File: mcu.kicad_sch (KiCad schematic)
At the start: 23 parts, among them J1 USB4105-GF-A-120, U1 STM32G473CEUx, Y1 ECS-240-6-37B-7KM-TR

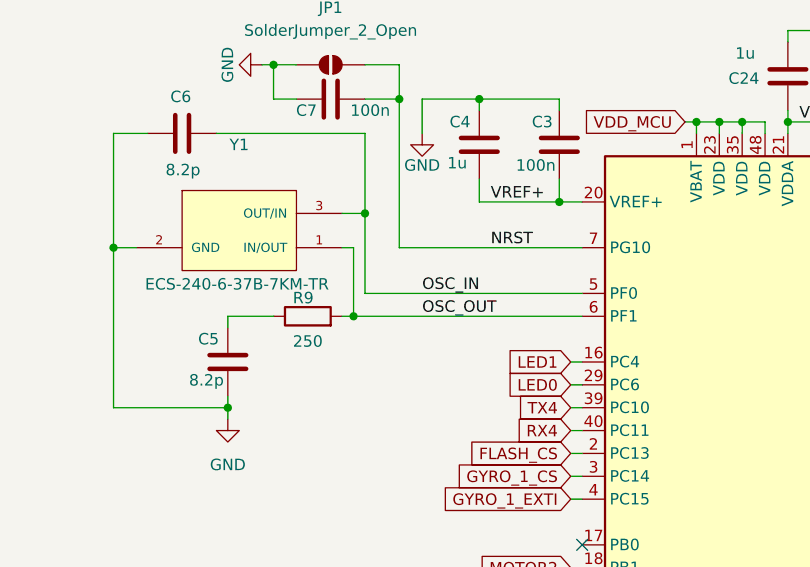
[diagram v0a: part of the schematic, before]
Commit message: Placed every components on one face only
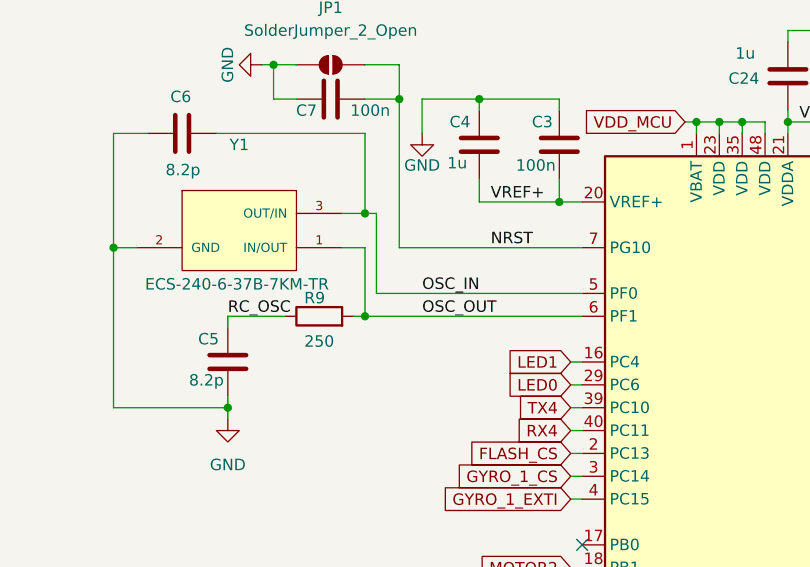
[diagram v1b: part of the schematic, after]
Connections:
- net RC_OSC: now reaches C5.1, R9.1
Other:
- moved on the sheet: R9
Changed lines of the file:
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@@
 	)
 	(junction
-		(at 55.88 100.33)
-		(diameter 0)
-		(color 0 0 0 0)
-	)
-	(junction
 		(at 120.65 125.73)
 		(diameter 0)
@@
 	)
 	(junction
+		(at 57.15 100.33)
+		(diameter 0)
+		(color 0 0 0 0)
+	)
+	(junction
 		(at 57.15 88.9)
 		(diameter 0)
@@
 	(wire
 		(pts
-			(xy 57.15 88.9) (xy 57.15 97.79)
+			(xy 58.42 88.9) (xy 58.42 97.79)
 		)
 		(stroke
@@
 	(wire
 		(pts
-			(xy 54.61 100.33) (xy 55.88 100.33)
-		)
-		(stroke
-			(width 0)
-			(type default)
-		)
-	)
-	(wire
-		(pts
 			(xy 80.01 138.43) (xy 81.28 138.43)
 		)
@@
 	(wire
 		(pts
-			(xy 55.88 100.33) (xy 81.28 100.33)
-		)
-		(stroke
-			(width 0)
-			(type default)
-		)
-	)
-	(wire
-		(pts
 			(xy 116.84 87.63) (xy 118.11 87.63)
 		)
@@
 	(wire
 		(pts
+			(xy 57.15 100.33) (xy 81.28 100.33)
+		)
+		(stroke
+			(width 0)
+			(type default)
+		)
+	)
+	(wire
+		(pts
 			(xy 78.74 76.2) (xy 78.74 77.47)
 		)
@@
 	(wire
 		(pts
+			(xy 58.42 88.9) (xy 57.15 88.9)
+		)
+		(stroke
+			(width 0)
+			(type default)
+		)
+	)
+	(wire
+		(pts
 			(xy 116.84 95.25) (xy 118.11 95.25)
 		)
@@
 	(wire
 		(pts
-			(xy 54.61 92.71) (xy 55.88 92.71)
+			(xy 54.61 92.71) (xy 57.15 92.71)
 		)
 		(stroke
@@
 	(wire
 		(pts
-			(xy 55.88 92.71) (xy 55.88 100.33)
+			(xy 57.15 92.71) (xy 57.15 100.33)
 		)
 		(stroke
@@
 	(wire
 		(pts
-			(xy 81.28 97.79) (xy 57.15 97.79)
+			(xy 81.28 97.79) (xy 58.42 97.79)
 		)
 		(stroke
@@
 	(wire
 		(pts
-			(xy 41.91 100.33) (xy 46.99 100.33)
+			(xy 41.91 100.33) (xy 48.26 100.33)
 		)
 		(stroke
@@
 	(wire
 		(pts
+			(xy 57.15 100.33) (xy 55.88 100.33)
+		)
+		(stroke
+			(width 0)
+			(type default)
+		)
+	)
+	(wire
+		(pts
 			(xy 93.98 78.74) (xy 93.98 80.01)
 		)
@@
 		)
 	)
+	(label "RC_OSC"
+		(at 41.91 100.33 0)
+		(effects
+			(font
+				(size 1.27 1.27)
+			)
+			(justify left bottom)
+		)
+	)
 	(label "USB_DIFF+"
 		(at 198.12 107.95 0)
@@
 	(symbol
 		(lib_id "Device:R")
-		(at 50.8 100.33 90)
+		(at 52.07 100.33 90)
 		(unit 1)
 		(exclude_from_sim no)
@@
 		(dnp no)
 		(property "Reference" "R9"
-			(at 50.292 98.298 90)
+			(at 51.562 98.298 90)
 			(effects
 				(font
@@
 		)
 		(property "Value" "250"
-			(at 50.8 103.124 90)
+			(at 52.07 103.124 90)
 			(effects
 				(font
@@
 		)
 		(property "Footprint" "Resistor_SMD:R_0402_1005Metric"
-			(at 50.8 102.108 90)
+			(at 52.07 102.108 90)
 			(effects
 				(font
@@
 		)
 		(property "Datasheet" "~"
-			(at 50.8 100.33 0)
+			(at 52.07 100.33 0)
 			(effects
 				(font
@@
 		)
 		(property "Description" "Resistor"
-			(at 50.8 100.33 0)
+			(at 52.07 100.33 0)
 			(effects
 				(font

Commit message: routing...
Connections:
- net GND: now also R15.1; no longer JP2.1 (A)
- net MOTOR1: now also JP2.2 (B)
- net VDD_MCU: now also JP2.1 (A)
- removed net BOOT0: JP2.2 (B), R15.1
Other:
- note added: "Se renseigner sur le type de pad smd en fabrication"
- moved on the sheet: JP2, R15, R22

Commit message: routing
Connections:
- net SWCLK-JTCK: now reaches U1.37 (PA14)
- net BEEPER renamed BZ
- net PINIO1 renamed SWDIO-JTMS
- no-connect marks 4 -> 3
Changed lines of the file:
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@@
 		(at 234.95 106.68)
 	)
-	(no_connect
-		(at 116.84 123.19)
-	)
 	(wire
 		(pts
@@
 		(pts
 			(xy 58.42 146.05) (xy 81.28 146.05)
+		)
+		(stroke
+			(width 0)
+			(type default)
+		)
+	)
+	(wire
+		(pts
+			(xy 116.84 123.19) (xy 118.11 123.19)
 		)
 		(stroke
@@
 		)
 	)
-	(global_label "PINIO1"
+	(global_label "SPI1_SDI"
+		(shape input)
+		(at 118.11 102.87 0)
+		(fields_autoplaced yes)
+		(effects
+			(font
+				(size 1.27 1.27)
+			)
+			(justify left)
+		)
+		(property "Intersheetrefs" "${INTERSHEET_REFS}"
+			(at 129.4409 102.87 0)
+			(effects
+				(font
+					(size 1.27 1.27)
+				)
+				(justify left)
+				(hide yes)
+			)
+		)
+	)
+	(global_label "SWCLK-JTCK"
+		(shape input)
+		(at 118.11 123.19 0)
+		(fields_autoplaced yes)
+		(effects
+			(font
+				(size 1.27 1.27)
+			)
+			(justify left)
+		)
+		(property "Intersheetrefs" "${INTERSHEET_REFS}"
+			(at 133.3718 123.19 0)
+			(effects
+				(font
+					(size 1.27 1.27)
+				)
+				(justify left)
+				(hide yes)
+			)
+		)
+	)
+	(global_label "VDD_MCU"
+		(shape input)
+		(at 58.42 162.56 270)
+		(fields_autoplaced yes)
+		(effects
+			(font
+				(size 1.27 1.27)
+			)
+			(justify right)
+		)
+		(property "Intersheetrefs" "${INTERSHEET_REFS}"
+			(at 58.42 174.1933 90)
+			(effects
+				(font
+					(size 1.27 1.27)
+				)
+				(justify right)
+				(hide yes)
+			)
+		)
+	)
+	(global_label "SPI2_SD0"
+		(shape input)
+		(at 80.01 163.83 180)
+		(fields_autoplaced yes)
+		(effects
+			(font
+				(size 1.27 1.27)
+			)
+			(justify right)
+		)
+		(property "Intersheetrefs" "${INTERSHEET_REFS}"
+			(at 68.0744 163.83 0)
+			(effects
+				(font
+					(size 1.27 1.27)
+				)
+				(justify right)
+				(hide yes)
+			)
+		)
+	)
+	(global_label "BZ"
+		(shape input)
+		(at 118.11 107.95 0)
+		(fields_autoplaced yes)
+		(effects
+			(font
+				(size 1.27 1.27)
+			)
+			(justify left)
+		)
+		(property "Intersheetrefs" "${INTERSHEET_REFS}"
+			(at 123.5747 107.95 0)
+			(effects
+				(font
+					(size 1.27 1.27)
+				)
+				(justify left)
+				(hide yes)
+			)
+		)
+	)
+	(global_label "5V_USB"
+		(shape input)
+		(at 237.49 101.6 0)
+		(fields_autoplaced yes)
+		(effects
+			(font
+				(size 1.27 1.27)
+			)
+			(justify left)
+		)
+		(property "Intersheetrefs" "${INTERSHEET_REFS}"
+			(at 247.5509 101.6 0)
+			(effects
+				(font
+					(size 1.27 1.27)
+				)
+				(justify left)
+				(hide yes)
+			)
+		)
+	)
+	(global_label "TX3"
+		(shape input)
+		(at 80.01 151.13 180)
+		(fields_autoplaced yes)
+		(effects
+			(font
+				(size 1.27 1.27)
+			)
+			(justify right)
+		)
+		(property "Intersheetrefs" "${INTERSHEET_REFS}"
+			(at 73.6382 151.13 0)
+			(effects
+				(font
+					(size 1.27 1.27)
+				)
+				(justify right)
+				(hide yes)
+			)
+		)
+	)
+	(global_label "SWDIO-JTMS"
 		(shape input)
 		(at 118.11 120.65 0)
@@
 		)
 		(property "Intersheetrefs" "${INTERSHEET_REFS}"
-			(at 127.4453 120.65 0)
+			(at 133.1299 120.65 0)
 			(effects
 				(font
@@
 				(hide yes)
 			)
-		)
-	)
-	(global_label "SPI1_SDI"
-		(shape input)
-		(at 118.11 102.87 0)
-		(fields_autoplaced yes)
-		(effects
-			(font
-				(size 1.27 1.27)
-			)
-			(justify left)
-		)
-		(property "Intersheetrefs" "${INTERSHEET_REFS}"
-			(at 129.4409 102.87 0)
-			(effects
-				(font
-					(size 1.27 1.27)
-				)
-				(justify left)
-				(hide yes)
-			)
-		)
-	)
-	(global_label "VDD_MCU"
-		(shape input)
-		(at 58.42 162.56 270)
-		(fields_autoplaced yes)
-		(effects
-			(font
-				(size 1.27 1.27)
-			)
-			(justify right)
-		)
-		(property "Intersheetrefs" "${INTERSHEET_REFS}"
-			(at 58.42 174.1933 90)
-			(effects
-				(font
-					(size 1.27 1.27)
-				)
-				(justify right)
-				(hide yes)
-			)
-		)
-	)
-	(global_label "SPI2_SD0"
-		(shape input)
-		(at 80.01 163.83 180)
-		(fields_autoplaced yes)
-		(effects
-			(font
-				(size 1.27 1.27)
-			)
-			(justify right)
-		)
-		(property "Intersheetrefs" "${INTERSHEET_REFS}"
-			(at 68.0744 163.83 0)
-			(effects
-				(font
-					(size 1.27 1.27)
-				)
-				(justify right)
-				(hide yes)
-			)
-		)
-	)
-	(global_label "BEEPER"
-		(shape input)
-		(at 118.11 107.95 0)
-		(fields_autoplaced yes)
-		(effects
-			(font
-				(size 1.27 1.27)
-			)
-			(justify left)
-		)
-		(property "Intersheetrefs" "${INTERSHEET_REFS}"
-			(at 128.3522 107.95 0)
-			(effects
-				(font
-					(size 1.27 1.27)
-				)
-				(justify left)
-				(hide yes)
-			)
-		)
-	)
-	(global_label "5V_USB"
-		(shape input)
-		(at 237.49 101.6 0)
-		(fields_autoplaced yes)
-		(effects
-			(font
-				(size 1.27 1.27)
-			)
-			(justify left)
-		)
-		(property "Intersheetrefs" "${INTERSHEET_REFS}"
-			(at 247.5509 101.6 0)
-			(effects
-				(font
-					(size 1.27 1.27)
-				)
-				(justify left)
-				(hide yes)
-			)
-		)
-	)
-	(global_label "TX3"
-		(shape input)
-		(at 80.01 151.13 180)
-		(fields_autoplaced yes)
-		(effects
-			(font
-				(size 1.27 1.27)
-			)
-			(justify right)
-		)
-		(property "Intersheetrefs" "${INTERSHEET_REFS}"
-			(at 73.6382 151.13 0)
-			(effects
-				(font
-					(size 1.27 1.27)
-				)
-				(justify right)
-				(hide yes)
-			)

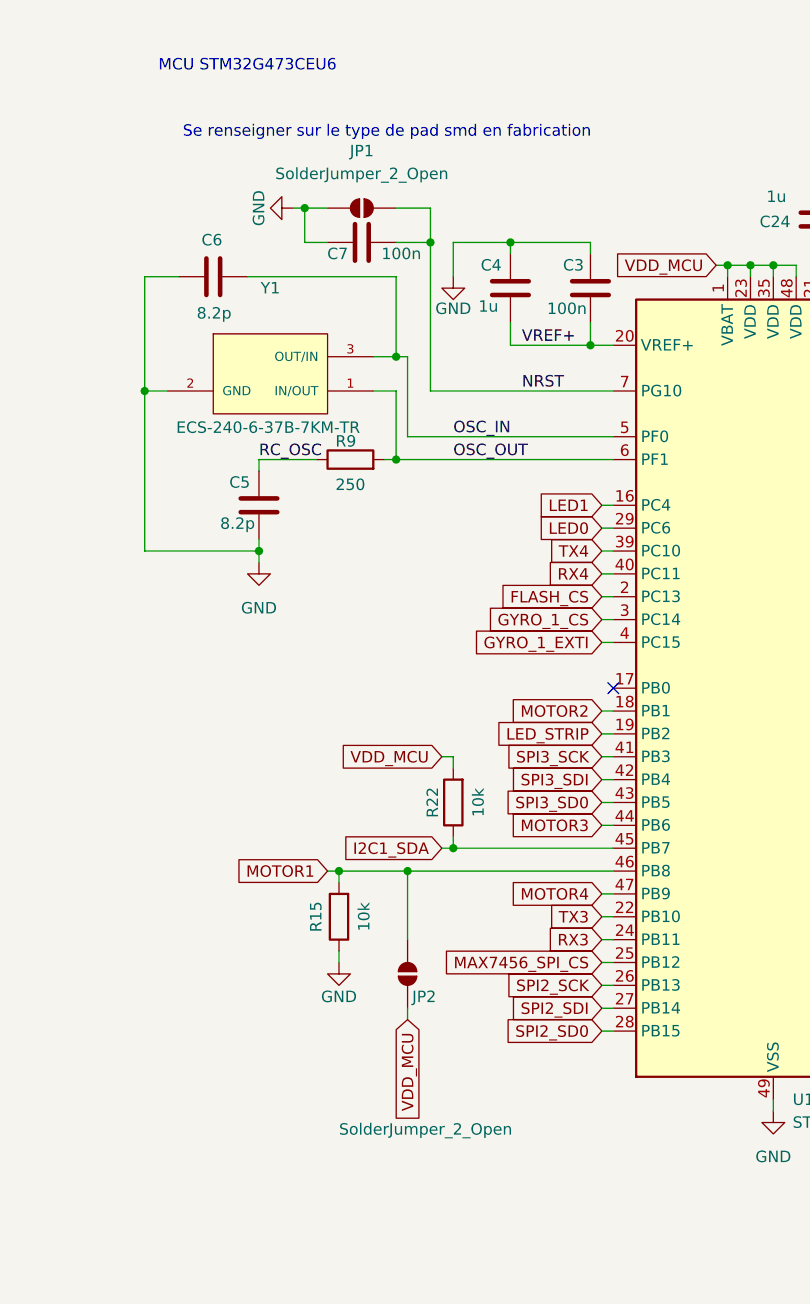
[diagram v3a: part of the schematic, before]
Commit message: Update footprint references and component values in schematic files
- Changed footprint property for a component in mcu.kicad_sch from "Package_DFN_QFN:QFN-48-1EP_7x7mm_P0.5mm_EP5.6x5.6mm" to "fcg4_fp:QFN-48-1EP_7x7mm_P0.5mm_EP5.6x5.6mm".
- Updated value property for a component in mcu.kicad_sch from "SolderJumper_2_Open" to "BOOT".
- Changed value property for another component in mcu.kicad_sch from "SolderJumper_2_Open" to "RESET".
- Modified footprint property for a component in sensor.kicad_sch from "ProLib_pcs_2026-02-12:SENSOR-SMD_SPL06-001" to "fcg4_fp:SENSOR-SMD_SPL06-001".
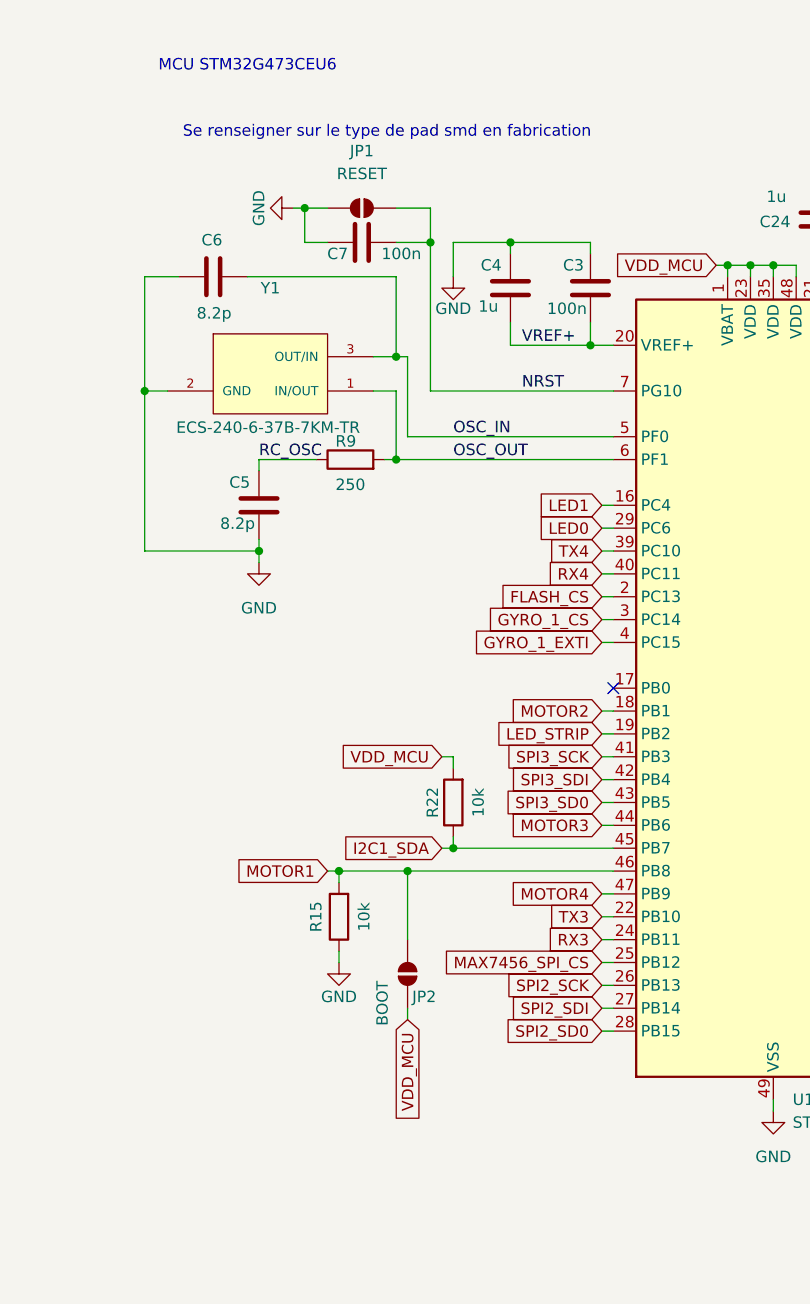
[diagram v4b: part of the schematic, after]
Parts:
- JP1: value SolderJumper_2_Open -> RESET
- JP2: value SolderJumper_2_Open -> BOOT
- U1: footprint Package_DFN_QFN:QFN-48-1EP_7x7mm_P0.5mm_EP5.6x5.6mm -> fcg4_fp:QFN-48-1EP_7x7mm_P0.5mm_EP5.6x5.6mm
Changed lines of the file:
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@@
 			)
 		)
-		(property "Footprint" "Package_DFN_QFN:QFN-48-1EP_7x7mm_P0.5mm_EP5.6x5.6mm"
+		(property "Footprint" "fcg4_fp:QFN-48-1EP_7x7mm_P0.5mm_EP5.6x5.6mm"
 			(at 83.82 168.91 0)
 			(effects
@@
 			)
 		)
-		(property "Value" "SolderJumper_2_Open"
-			(at 50.8 174.752 90)
+		(property "Value" "BOOT"
+			(at 55.626 158.242 0)
 			(effects
 				(font
@@
 			)
 		)
-		(property "Value" "SolderJumper_2_Open"
+		(property "Value" "RESET"
 			(at 53.34 68.58 0)
 			(effects

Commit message: Update component properties in schematics with manufacturer details and datasheets
- Added manufacturer name, part number, and LCSC part name for various components in mcu.kicad_sch, power.kicad_sch, and sensor.kicad_sch.
- Updated datasheet links for components to point to the correct URLs.
- Ensured all new properties are hidden in the schematic view.
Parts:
- C10, C11, C25, C3, C7, C8, C9: LCSC Part Name (none) -> C77020; Manufacturer_Name (none) -> muRata; Manufacturer_Part_Number (none) -> GRM155R71H104KE14D
- C24, C4: LCSC Part Name (none) -> C1518208; Manufacturer_Name (none) -> muRata; Manufacturer_Part_Number (none) -> GRM155R61H105KE05D
- C5, C6: LCSC Part Name (none) -> C76984; Manufacturer_Name (none) -> muRata; Manufacturer_Part_Number (none) -> GRM1555C1H8R2CA01D

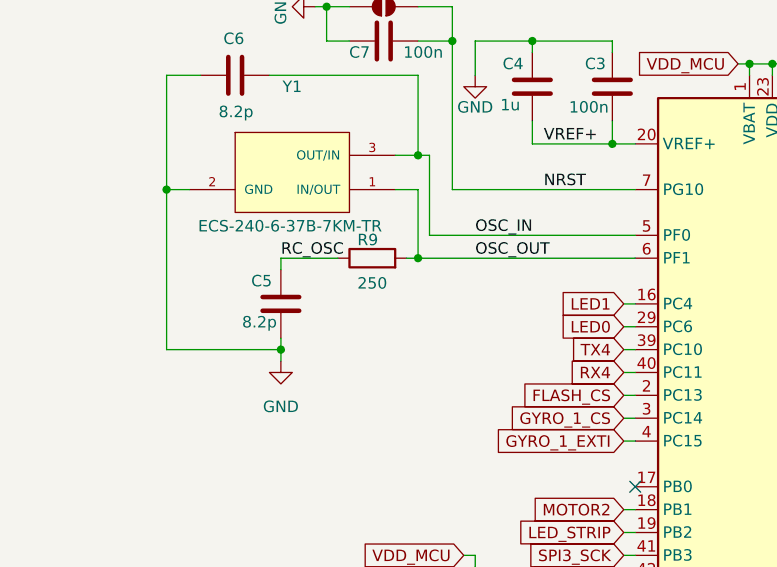
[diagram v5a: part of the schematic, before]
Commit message: Almost completed! Update component properties in sensor schematic
- Added datasheets, LCSC part names, manufacturer names, and manufacturer part numbers for various components in the sensor.kicad_sch file.
- Updated the datasheet links for components to point to the correct URLs.
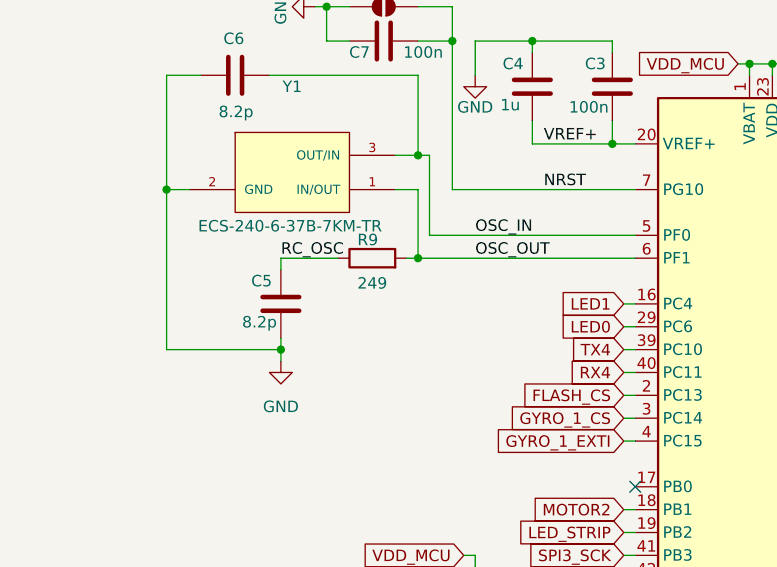
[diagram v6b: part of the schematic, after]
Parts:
- FL1: LCSC Part Name (none) -> C88987; Manufacturer_Name (none) -> muRata; Manufacturer_Part_Number (none) -> BLM18RK601SN1D
- J1: LCSC Part Name (none) -> C5184243; Manufacturer_Name (none) -> Global Connector Technology; Manufacturer_Part_Number (none) -> USB4105-GF-A-120
- R10, R11: LCSC Part Name (none) -> C105872; Manufacturer_Name (none) -> YAGEO; Manufacturer_Part_Number (none) -> RC0402FR-075K1L
- R15, R22, R23: LCSC Part Name (none) -> C60490; Manufacturer_Name (none) -> YAGEO; Manufacturer_Part_Number (none) -> RC0402FR-0710KL
- R9: value 250 -> 249; LCSC Part Name (none) -> C185439; Manufacturer_Name (none) -> YAGEO; Manufacturer_Part_Number (none) -> RC0402FR-07249RL
- U1: LCSC Part Name (none) -> C1342773; Manufacturer_Name (none) -> ST; Manufacturer_Part_Number (none) -> STM32G473CEU6
- Y1: Manufacturer_Name (none) -> ECS; Manufacturer_Part_Number (none) -> ECS-240-6-37B-7KM-TR; Mouser Part Number (none) -> 520-240-6-37B-7KM-TR
